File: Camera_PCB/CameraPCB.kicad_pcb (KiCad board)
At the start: 6 copper layers, 162 parts, among them J1 MIPI-CSI2, J2 USB_A, J3 SDA, J4 UART_0, J5 UART_2, J6 USB_C_Receptacle_PowerOnly_6P, SW1 PWR, SW2 RST, U1 AXP203, U2 V3s-eLQFP128, U3 TPS63020, U4 TPS63020, Y2 32.768kHz XTAL, Y4 24MHz XTAL

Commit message: more schematic changes, added solder bridges, etc
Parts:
- added H1: MountingHole, MountingHole:MountingHole_2.2mm_M2, F.Cu at (176.6, 68.0)
- added H2: MountingHole, MountingHole:MountingHole_2.2mm_M2, F.Cu at (119.0, 68.0)
- added H3: MountingHole, MountingHole:MountingHole_2.2mm_M2, F.Cu at (119.0, 130.0)
- added H4: MountingHole, MountingHole:MountingHole_2.2mm_M2, F.Cu at (176.6, 130.0)
- added JP1: ~, Jumper:SolderJumper-2_P1.3mm_Open_Pad1.0x1.5mm, B.Cu at (144.9, 119.4)
- added JP2: ~, Jumper:SolderJumper-2_P1.3mm_Open_Pad1.0x1.5mm, B.Cu at (123.1, 112.5)
- added JP3: ~, Jumper:SolderJumper-2_P1.3mm_Open_Pad1.0x1.5mm, B.Cu at (120.2, 120.0)
- added JP4: ~, Jumper:SolderJumper-2_P1.3mm_Open_Pad1.0x1.5mm, B.Cu at (132.1, 103.5)
- added JP5: ~, Jumper:SolderJumper-2_P1.3mm_Open_Pad1.0x1.5mm, B.Cu at (142.5, 149.2)
- added JP6: ~, Jumper:SolderJumper-2_P1.3mm_Open_Pad1.0x1.5mm, B.Cu at (161.7, 137.5)
- C2, C3, C35, C36, C42, C43, C44, C45, C48, C49, C5, C50, C51, C52, C53, C54, C55, C56, C57, C58, C6, C61, C62, C63, C64, C65, C66, C67, C71, C73, C74, R14, R15, R22, R23, R24, R25, R26, R27, TP1, TP12, TP13, TP16, TP17, TP18, TP19, TP2, TP20, TP21, TP22, TP23, TP24, TP3, TP4, TP6, TP7, TP8, U3, U4: moved to B.Cu
- NT1: footprint NetTie:NetTie-2_SMD_Pad2.0mm -> NetTie:NetTie-2_SMD_Pad0.5mm; moved to B.Cu
- R16, R17: moved to F.Cu
- moved TP30 220.0 mm to (277.4, 66.1)
- moved TP32 220.0 mm to (277.4, 73.2)
- moved TP14 220.0 mm to (273.9, 66.1)
- moved TP15 220.0 mm to (273.9, 69.7)
- moved TP28 220.0 mm to (273.9, 73.2)
- moved TP29 220.0 mm to (273.9, 76.8)
- moved TP31 220.0 mm to (277.4, 69.7)
- moved C10 208.5 mm to (250.3, 66.1)
- moved C11 208.5 mm to (250.3, 68.6)
- moved C12 208.5 mm to (250.3, 71.1)
- moved C13 208.5 mm to (250.3, 73.6)
- moved C14 208.5 mm to (250.3, 76.1)
- moved C15 208.5 mm to (250.3, 78.6)
- moved C16 208.5 mm to (250.3, 81.1)
- moved C17 208.5 mm to (254.6, 61.0)
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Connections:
- C53 pad 1: HPVCC -> Net-(JP6-A)
- C54 pad 2: VDD-CPU -> Net-(JP3-A)
- C55 pad 2: VDD-CPU -> Net-(JP3-A)
- C56 pad 2: VCC-DRAM -> Net-(JP4-A)
- C57 pad 2: VCC-DRAM -> Net-(JP4-A)
- C61 pad 2: VCC-RTC -> Net-(JP1-A)
- C63 pad 2: AVCC -> Net-(JP2-A)
- C64 pad 1: HPVCC -> Net-(JP6-A)
- C65 pad 1: HPVCC -> Net-(JP6-A)
- C66 pad 1: HPVCC -> Net-(JP6-A)
- C67 pad 1: HPVCC -> Net-(JP6-A)
- C68 pad 1: +5V -> Net-(JP5-A)
- C69 pad 1: +5V -> Net-(JP5-A)
- C70 pad 1: +5V -> Net-(JP5-A)
- C71 pad 1: +5V -> Net-(JP5-A)
- C72 pad 1: +5V -> Net-(JP5-A)
- L8 pad 2: VDD-CPU -> Net-(JP3-A)
- L9 pad 2: VCC-DRAM -> Net-(JP4-A)
- R24 pad 1: +5V -> Net-(JP5-A)
- R26 pad 1: HPVCC -> Net-(JP6-A)
- TP21 pad 1: +5V -> Net-(JP5-A)
- TP22 pad 1: HPVCC -> Net-(JP6-A)
- TP3 pad 1: VDD-CPU -> Net-(JP3-A)
- TP4 pad 1: VCC-DRAM -> Net-(JP4-A)
- TP8 pad 1: VCC-RTC -> Net-(JP1-A)
- U1 pad 10: VDD-CPU -> Net-(JP3-A)
- U1 pad 12: AVCC -> Net-(JP2-A)
- U1 pad 17: VCC-DRAM -> Net-(JP4-A)
- U1 pad 28: VCC-RTC -> Net-(JP1-A)
- U3 pad 4: +5V -> Net-(JP5-A)
- U3 pad 5: +5V -> Net-(JP5-A)
- U4 pad 4: HPVCC -> Net-(JP6-A)
- U4 pad 5: HPVCC -> Net-(JP6-A)
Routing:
- net SVREF: track 30.1 -> 0.00 mm
- net SZQ: track 29.9 -> 0.00 mm
- net VIPS: track 0.00 -> 29.4 mm, vias 0 -> 15
- net SDC0_D1: track 22.9 -> 0.00 mm
- net CSI_SDA: track 21.4 -> 0.00 mm
- net UART2_TX: track 21.3 -> 0.00 mm
- net SDC0_D0: track 20.7 -> 0.00 mm
- net Net-(JP3-A): track 0.00 -> 18.5 mm
- net (no net): track 17.1 -> 0.00 mm
- net MCSI_D0_P: track 0.00 -> 15.5 mm, vias 0 -> 2
- net MCSI_CK_N: track 0.00 -> 15.5 mm, vias 0 -> 2
- net Net-(U1-CHSENSE): track 0.00 -> 15.3 mm
- net MCSI_CK_P: track 0.00 -> 15.3 mm, vias 0 -> 2
- net VDD-CPU: track 15.2 -> 0.00 mm
- net X24MIN: track 15.2 -> 0.00 mm
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- added copper zone on B.Cu, net GND
- added copper zone on F.Cu, net GND
- added copper zone on In1.Cu, net GND
- added copper zone on In2.Cu, net GND
- added copper zone on In3.Cu, net GND
- added copper zone on In4.Cu, net GND
- removed copper zone on In1.Cu, net (none)
- removed copper zone on In2.Cu, net (none)
- removed copper zone on B.Cu, net +5V
- removed copper zone on In3.Cu, net VCC-DRAM
- removed copper zone on In4.Cu, net VDD-CPU
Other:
- board outline added: 65.6 x 70 mm

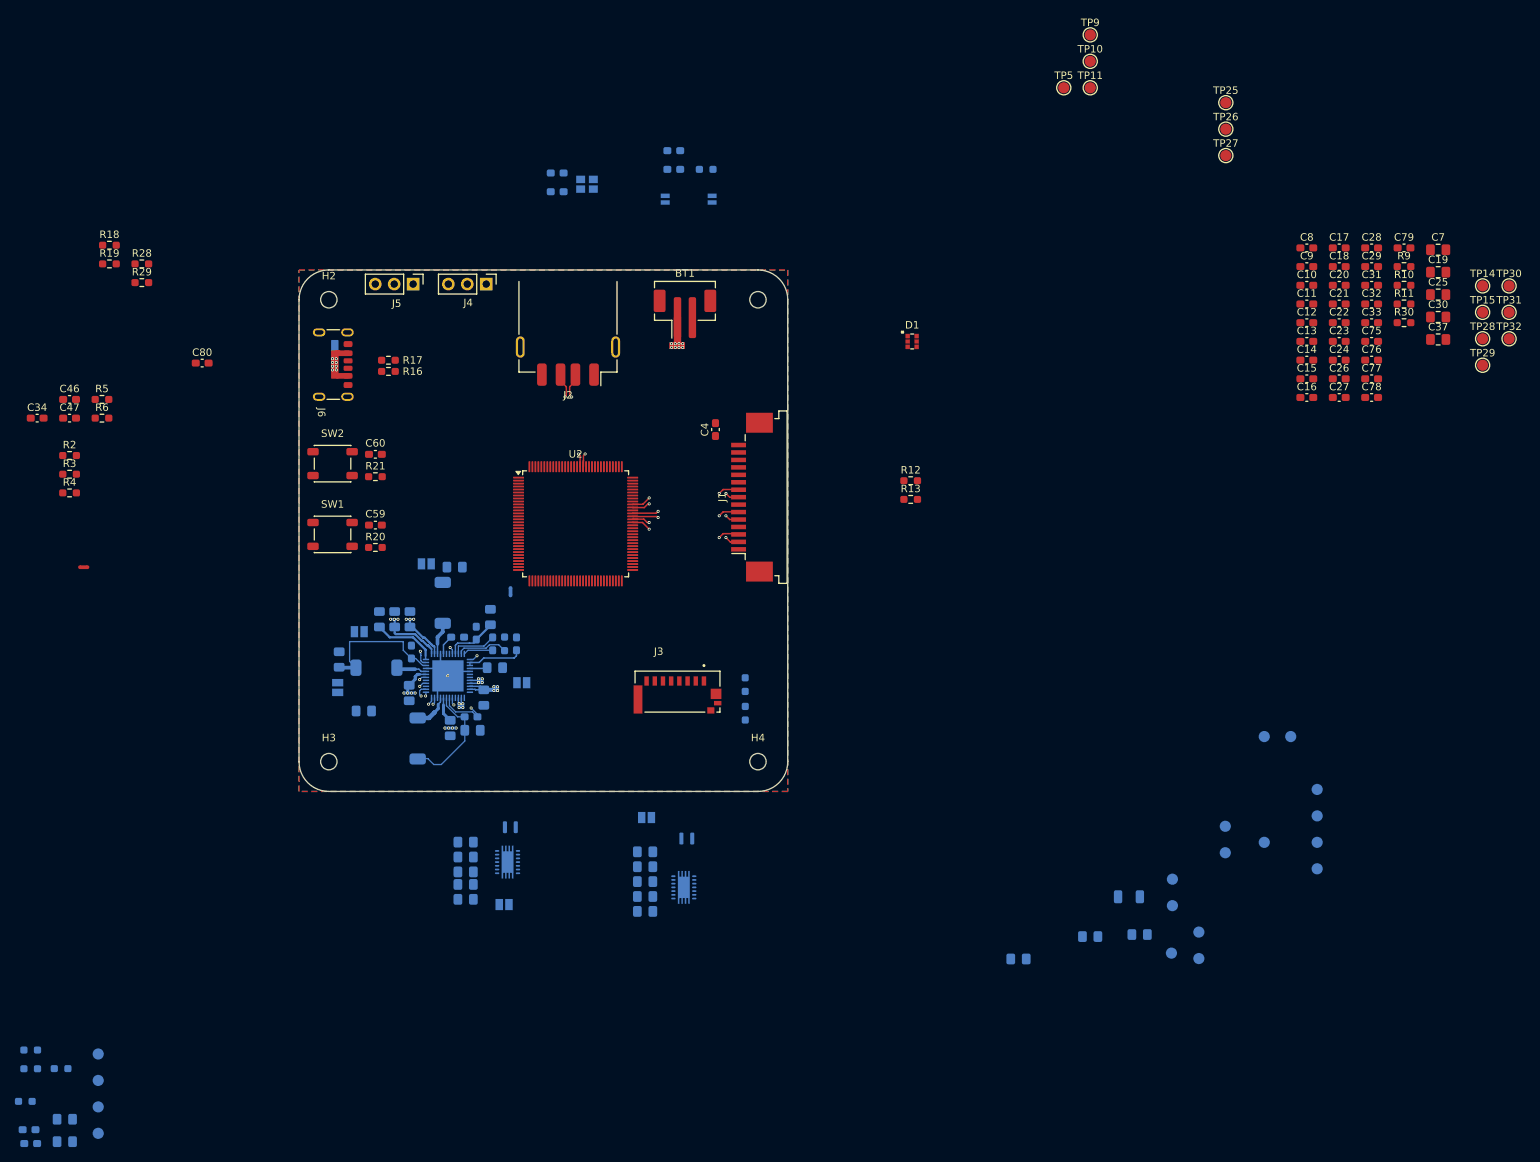
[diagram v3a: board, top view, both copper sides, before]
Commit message: PCB commit before reorganizing
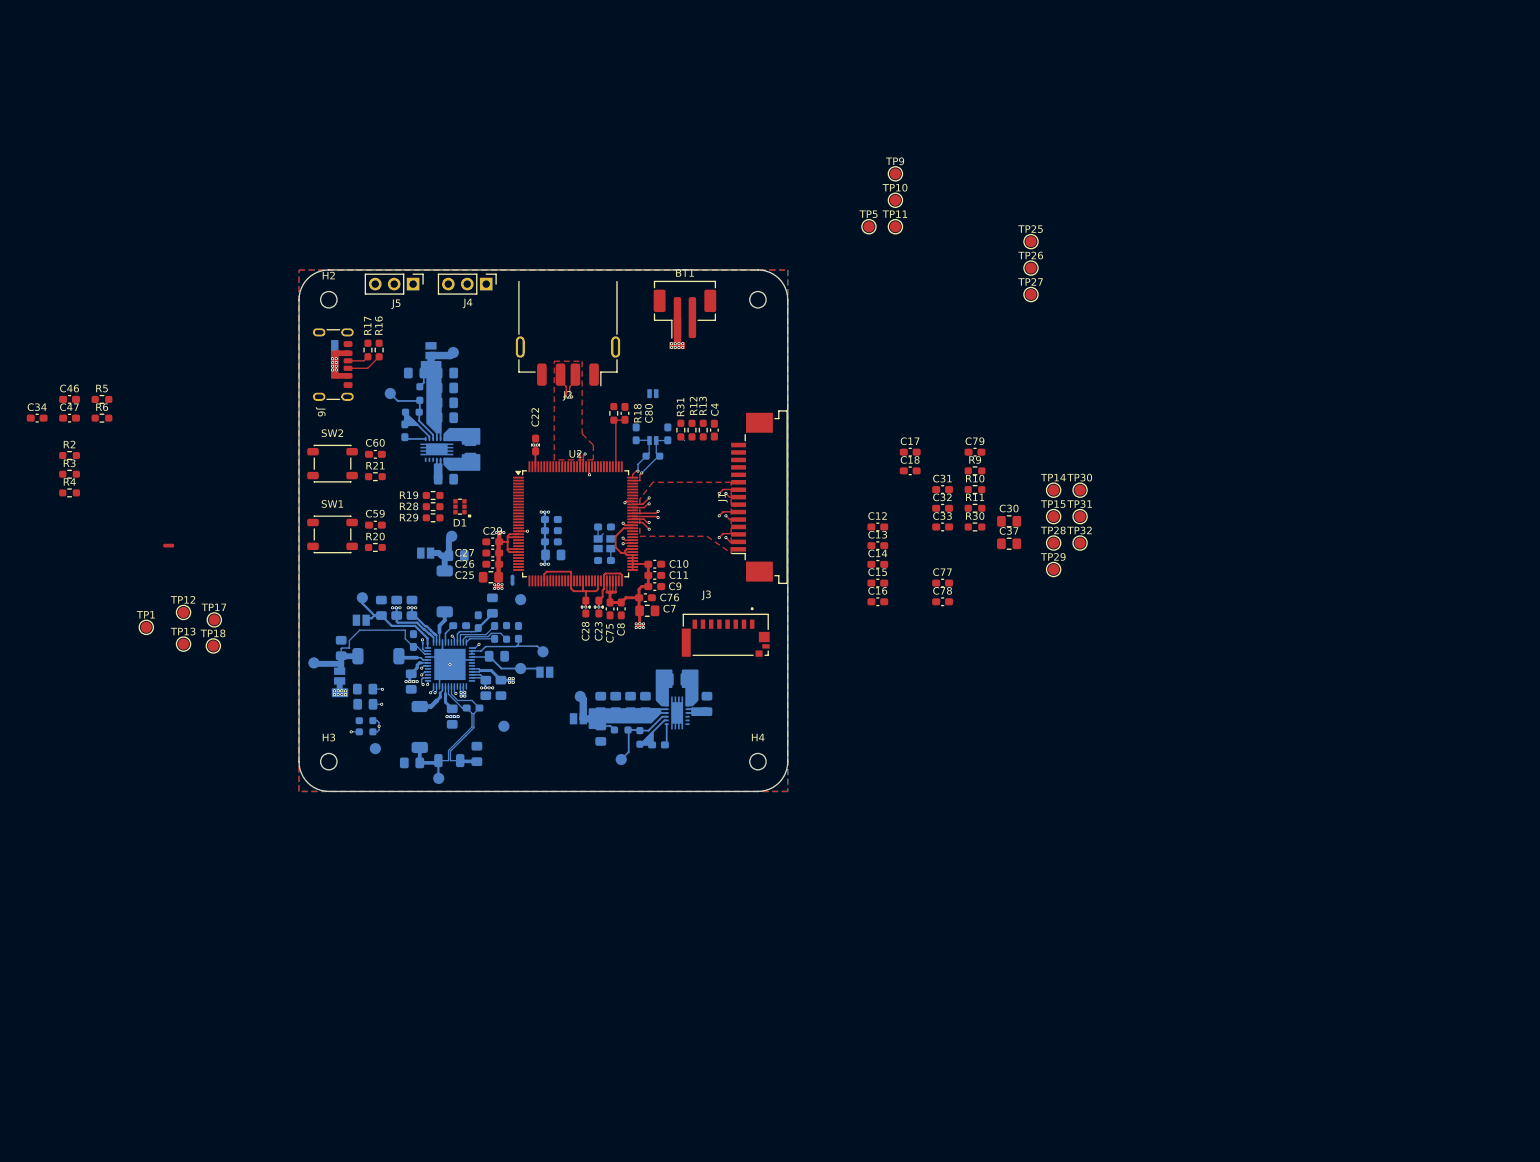
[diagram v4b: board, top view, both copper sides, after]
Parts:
- added R31: 4.7k, Resistor_SMD:R_0603_1608Metric_Pad0.98x0.95mm_HandSolder, F.Cu at (166.2, 85.5)
- C19, C20, C21, C24: moved to B.Cu
- TP1, TP12, TP13, TP17, TP18: moved to F.Cu
- moved TP13 155.1 mm to (99.5, 114.2)
- moved TP17 150.3 mm to (103.6, 111.0)
- moved TP12 149.5 mm to (99.5, 110.0)
- moved TP18 149.4 mm to (103.5, 114.5)
- moved TP1 144.4 mm to (94.5, 112.0)
- moved C25 132.7 mm to (140.8, 105.2)
- moved TP16 127.0 mm to (125.2, 128.2)
- moved C19 124.7 mm to (149.1, 102.2), turned to 180 degrees
- moved C29 123.6 mm to (141.0, 100.5)
- moved TP7 122.3 mm to (123.5, 108.0)
- moved TP3 119.7 mm to (117.0, 116.8)
- moved C7 116.7 mm to (161.8, 109.8), turned to 180 degrees
- moved C26 116.3 mm to (141.0, 103.5)
- moved C28 116.0 mm to (153.5, 109.2), turned to 90 degrees
- moved C27 115.5 mm to (141.0, 102.0)
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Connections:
- TP7 pad 1: AVCC -> Net-(JP2-A)
- Y2 pad 2: X32KOUT -> GND
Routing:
- net VDD-CPU: track 0.00 -> 165.8 mm, vias 0 -> 35
- net VCC-DRAM: track 0.00 -> 35.3 mm, vias 0 -> 6
- net Net-(JP5-A): track 0.00 -> 21.2 mm
- net Net-(JP6-A): track 0.00 -> 21.2 mm
- net VBAT: track 12.9 -> 30.2 mm, vias 13 -> 12
- net Net-(U4-FB): track 0.00 -> 10.4 mm
- net Net-(U3-FB): track 0.00 -> 10.4 mm
- net X32KOUT: track 0.00 -> 9.28 mm, vias 0 -> 1
- net VIPS: track 29.4 -> 37.4 mm, vias 15 -> 16
- net Net-(JP4-A): track 2.68 -> 10.6 mm
- net RESET: track 0.00 -> 7.88 mm
- net X32KIN: track 0.00 -> 7.87 mm, vias 0 -> 1
- net Net-(JP1-A): track 2.35 -> 10.1 mm
- net GND: track 7.80 -> 15.5 mm
- net Net-(JP2-A): track 8.79 -> 15.1 mm
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
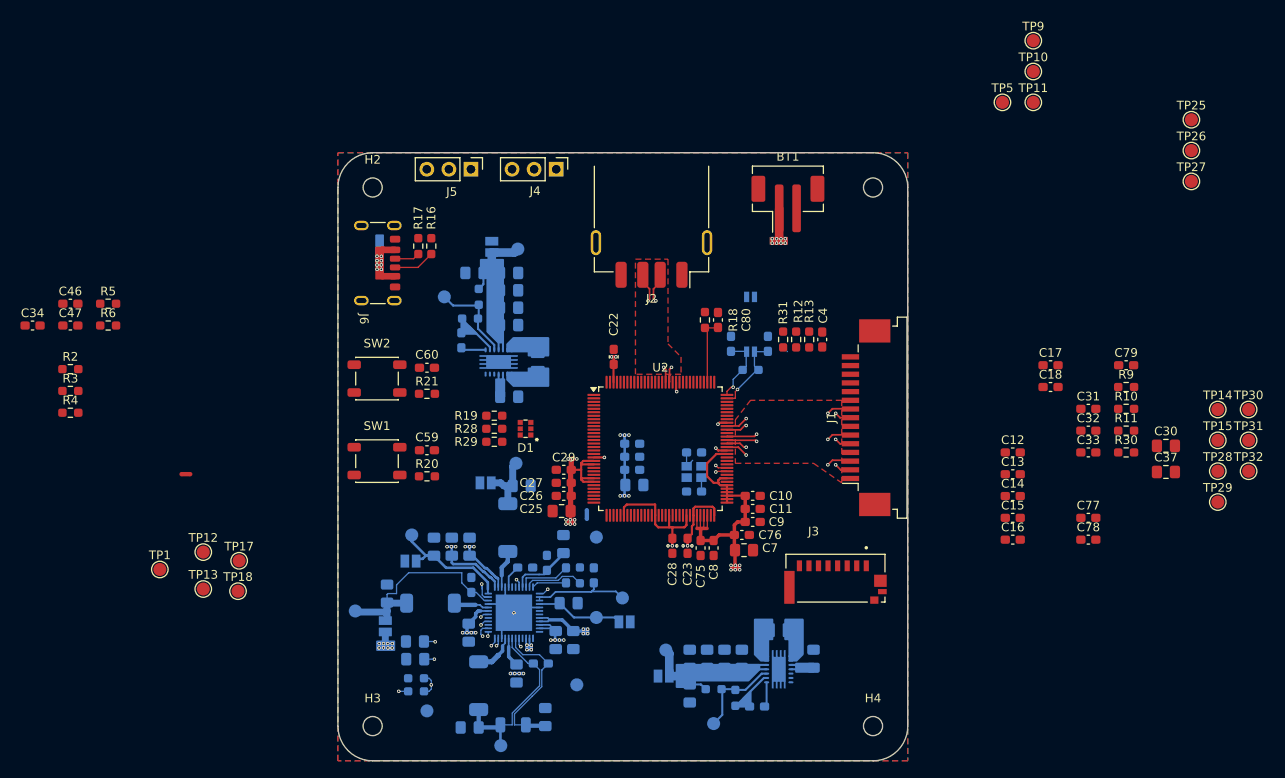
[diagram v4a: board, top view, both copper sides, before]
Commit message: Shrunk camera PCB and rearranged connectors. Everything on board. Not everything connected.
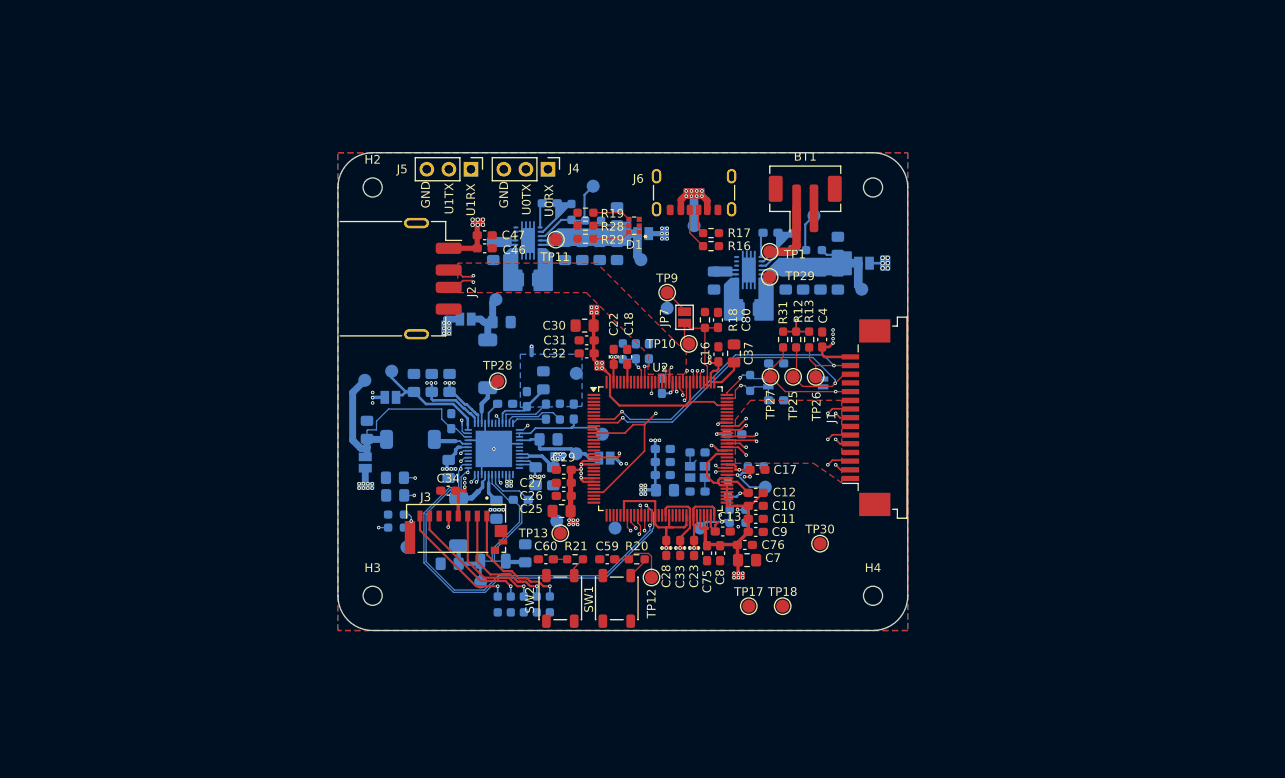
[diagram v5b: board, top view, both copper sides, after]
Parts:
- removed NT2: NetTie_2, NetTie:NetTie-2_SMD_Pad0.5mm
- added JP7: ~, Jumper:SolderJumper-2_P1.3mm_Open_Pad1.0x1.5mm, F.Cu at (154.9, 83.0)
- C14, C15, C77, C78, C79, R10, R11, R2, R3, R30, R4, R5, R6, R9, TP14, TP15, TP31, TP32, TP5: moved to B.Cu
- moved TP28 83.5 mm to (133.4, 90.3)
- moved TP1 79.2 mm to (164.7, 75.4)
- moved TP32 73.2 mm to (146.9, 107.2)
- moved TP31 68.6 mm to (152.9, 81.9)
- moved C30 68.3 mm to (143.4, 83.9)
- moved TP18 62.7 mm to (166.2, 116.2)
- moved R2 61.5 mm to (139.4, 116.0), turned to 90 degrees
- moved TP14 61.1 mm to (156.7, 107.2)
- moved TP24 59.6 mm to (169.8, 71.2), turned to 180 degrees
- moved R30 59.1 mm to (147.8, 86.9), turned to -90 degrees
- moved R5 59.1 mm to (136.4, 116.0), turned to 90 degrees
- moved R3 59.1 mm to (137.9, 116.0), turned to 90 degrees
- moved TP17 58.9 mm to (162.3, 116.2)
- moved C32 58.4 mm to (143.6, 87.1)
- moved C31 58.3 mm to (143.6, 85.6)
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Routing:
- net HPVCC: track 9.50 -> 227.5 mm, vias 3 -> 31
- net AVCC: track 0.00 -> 81.8 mm, vias 0 -> 7
- net VCC-DRAM: track 35.3 -> 112.4 mm, vias 6 -> 13
- net +5V: track 0.00 -> 56.8 mm, vias 0 -> 12
- net SDC0_D0: track 0.00 -> 50.7 mm, vias 0 -> 2
- net SDC0_D1: track 0.00 -> 48.3 mm, vias 0 -> 2
- net SDC0_D3: track 0.00 -> 48.3 mm, vias 0 -> 2
- net SDC0_CMD: track 0.00 -> 48.2 mm, vias 0 -> 2
- net TWI0_SCK: track 1.72 -> 49.7 mm, vias 1 -> 2
- net SDC0_D2: track 0.00 -> 47.9 mm, vias 0 -> 2
- net SDC0_CLK: track 0.00 -> 45.6 mm, vias 0 -> 2
- net TWI0_SDA: track 0.52 -> 45.5 mm, vias 1 -> 2
- net CSI_SCK: track 0.00 -> 44.0 mm, vias 0 -> 2
- net VBUS: track 10.2 -> 51.4 mm, vias 12 -> 13
- net CSI_SDA: track 0.00 -> 39.7 mm, vias 0 -> 2
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- added copper zone on B.Cu, net GNDA
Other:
- board size 65.6 x 70 mm -> 65.6 x 55 mm
- board text added: "GND"
- board text added: "U0RX"
- board text added: "U0TX"
- board text added: "U1RX"
- board text added: "U1TX"
